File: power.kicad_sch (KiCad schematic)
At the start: 36 parts, among them J1 CAN1 + power harness, J2 Aux bus harness, U1 TLV431A

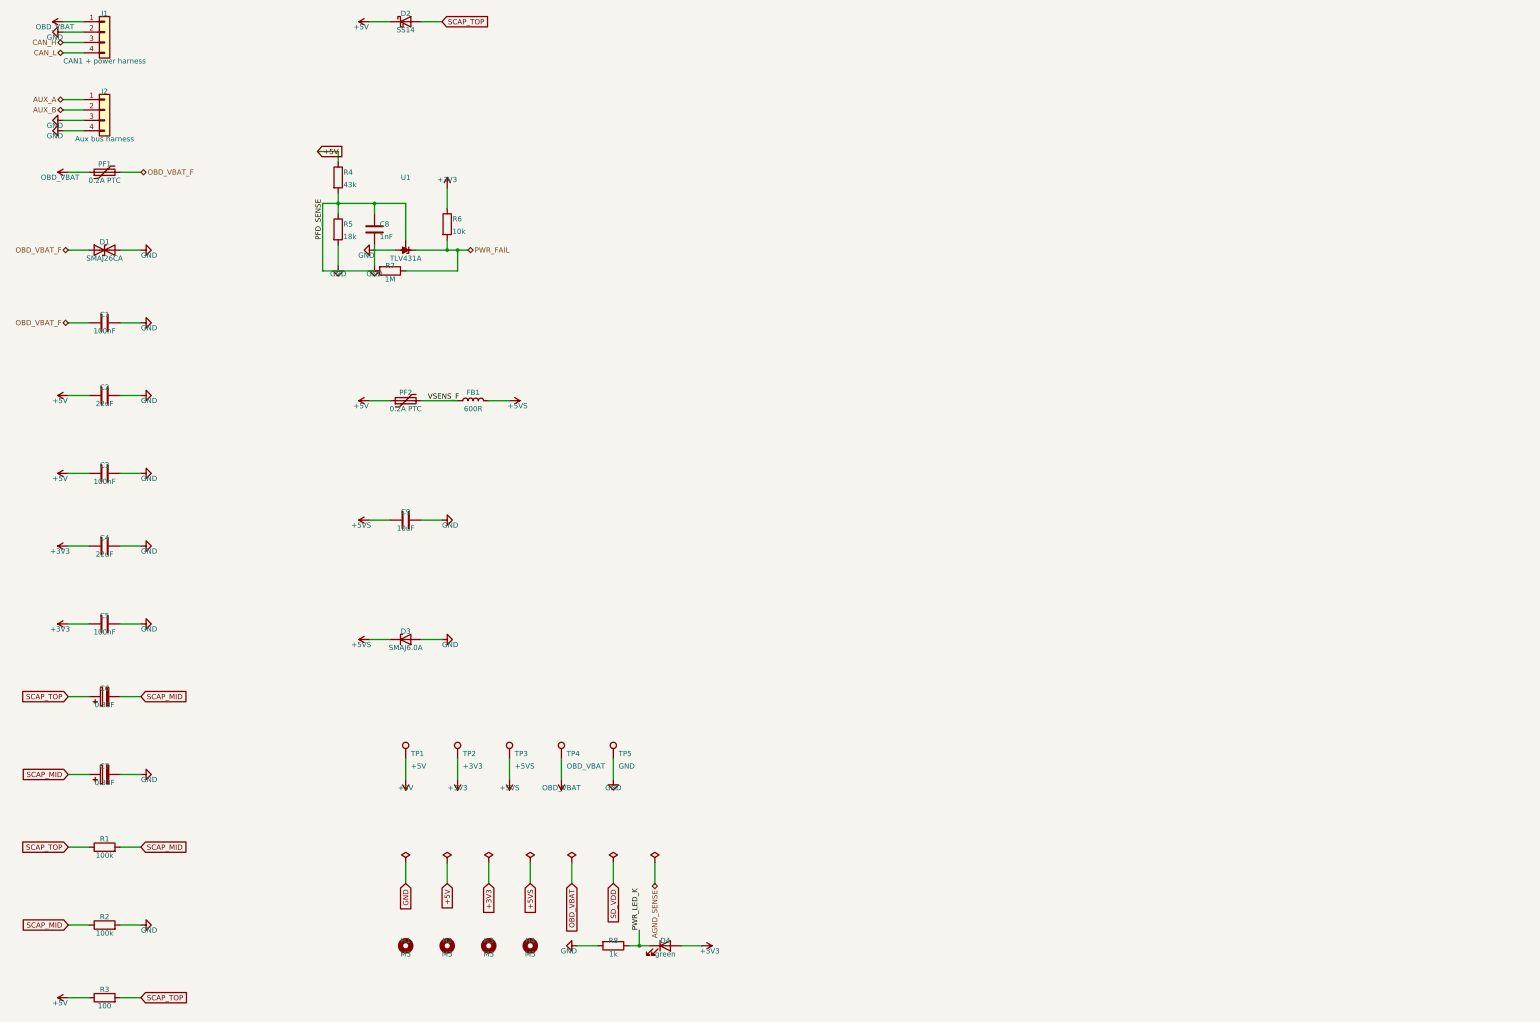
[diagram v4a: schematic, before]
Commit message: Make the schematic readable: wire the loose parts, stop text printing through symbols
Three things the drawing was doing badly, all now measured by a new
gen/audit_schematic.py rather than judged by eye.

LOOSE PARTS ARE WIRED NOW. A decoupling capacitor is a two-pin part with a
rail on each pin, and the column packer had no reason to put one next to
another -- so each came out as its own island with a net label at both ends,
twenty-odd of them down the edge of the power sheet. Electrically perfect,
visually a parts bin. build_ladders() groups the leftovers by which pair of
nets they sit across and draws each group as a proper ladder: one wire along
the top pins, one along the bottom, a junction at every rung and a power
symbol at each end. Nine groups across five sheets, including the supercap
bank and the battery monitor, and it removes two labels per part.

Grouping is on the actual pin GEOMETRY, not the symbol name, which is what
lets a balancing resistor share a ladder with the capacitor it balances while
keeping out a TVS diode whose pins are 1.3 mm closer together -- that one ERC
caught as two unconnected wire endpoints.

TEXT NO LONGER PRINTS THROUGH SYMBOLS. The offsets that place a reference and
a value work from the box around a part's PINS, and a symbol's graphic is
routinely drawn outside it. A power symbol's arrow therefore went straight
through its own name -- "+5VS" read "+2VS" at a glance, which is exactly how
somebody ends up probing the wrong rail -- and a capacitor lying on its side
has a y extent of exactly zero, so its reference and value printed across the
plates. Both now work from a floor on the body size. Rail names are also
centred on their own pin instead of drooping half a pitch onto the next one,
and the solder jumpers lost "(default OFF)" from their value into their note,
which is eighteen characters of text on a part 1.3 mm wide.

THE HAND-DRAWN BLOCKS WERE RE-SPACED to suit, because their tables were laid
out when the text sat closer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
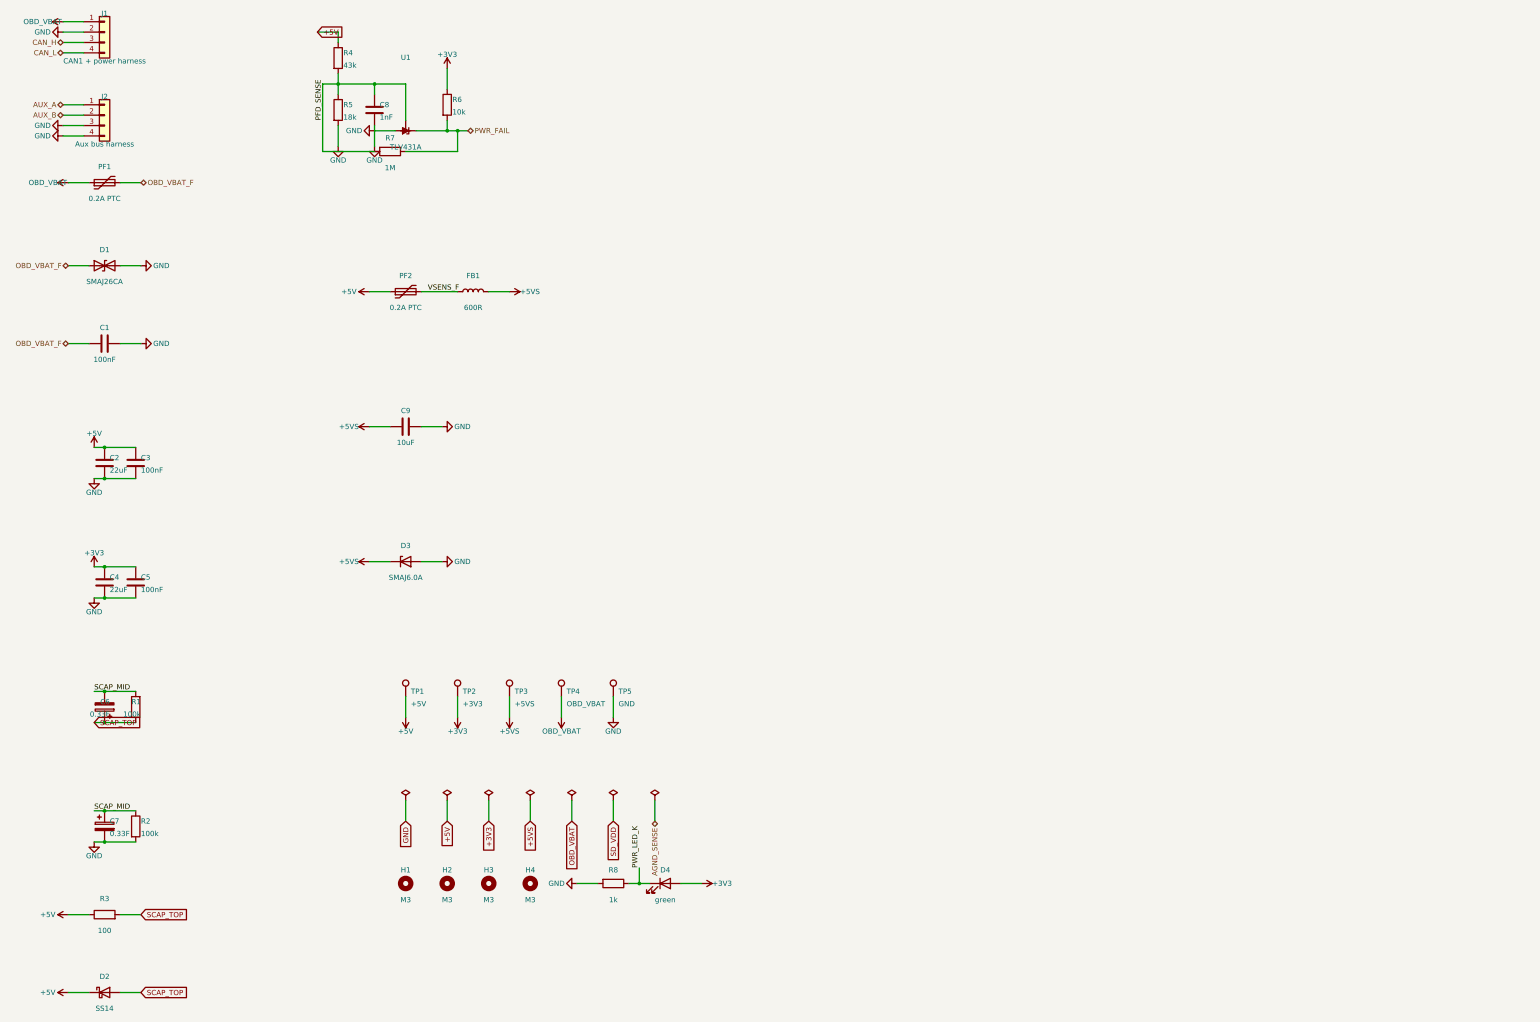
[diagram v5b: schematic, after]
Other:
- moved on the sheet: C1, C2, C3, C4, C5, C6, C7, C8, C9, D1, D2, D3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
